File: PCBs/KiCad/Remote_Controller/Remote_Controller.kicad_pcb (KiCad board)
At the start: 4 copper layers, 81 parts, among them J201 USB_C_Receptacle_USB2.0_16P, Q101 IRF7319, Q102 IRFML8244TRPBF, Q103 IRFML8244TRPBF, Q201 SS8050-G, Q202 SS8050-G, SW101 Power Switch, SW201 SW_Push, SW301 SW_Push, SW302 SW_Push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

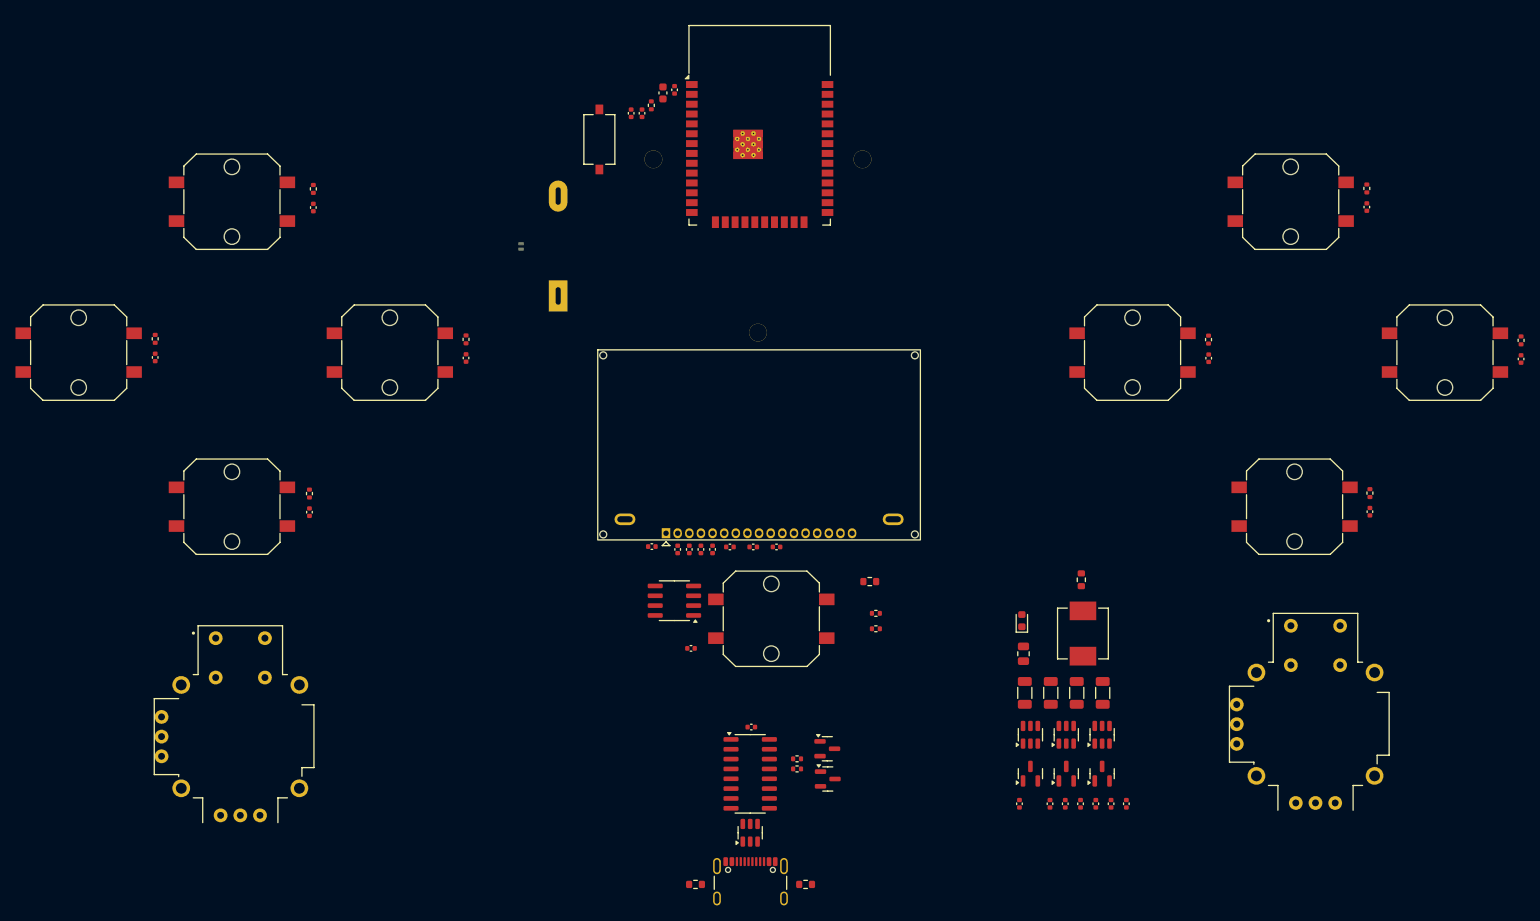
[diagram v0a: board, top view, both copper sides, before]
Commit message: Laid out components and PCB shape
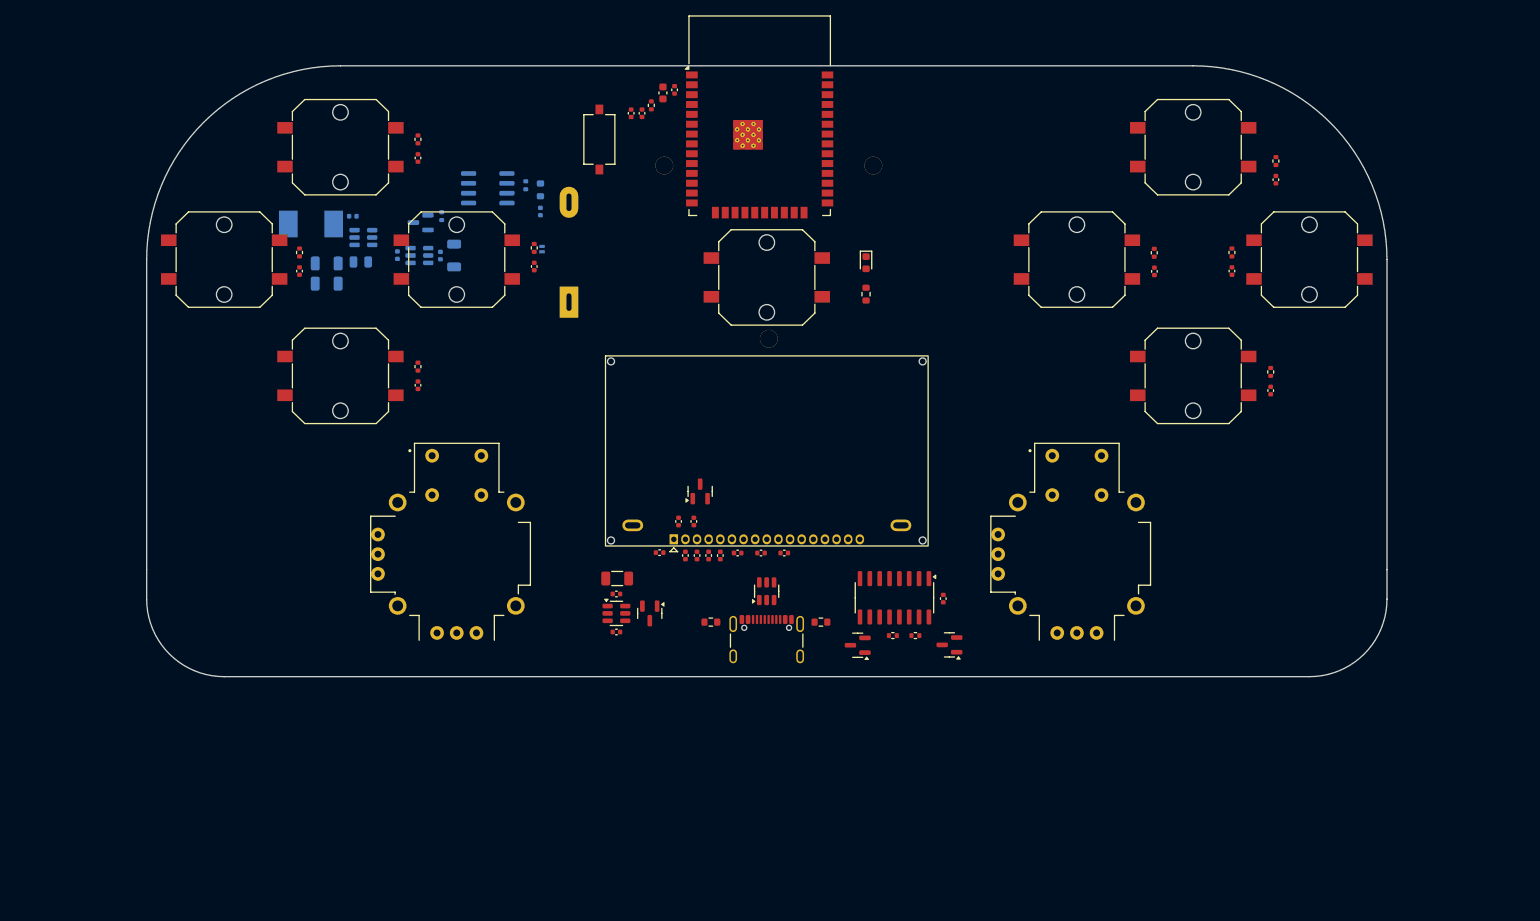
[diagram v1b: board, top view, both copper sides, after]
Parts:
- C101, C102, C103, C104, C105, C106, C107, C108, L101, Q101, Q102, R101, R102, R103, U101, U102: moved to B.Cu
- moved C101 114.6 mm to (87.6, 65.4), turned to 0 degrees
- moved L101 112.7 mm to (82.2, 66.4), turned to 180 degrees
- moved C106 110.0 mm to (93.3, 70.4), turned to -90 degrees
- moved C105 108.6 mm to (84.2, 71.5), turned to 0 degrees
- moved U101 107.3 mm to (89.0, 68.2), turned to 180 degrees
- moved C108 107.2 mm to (98.9, 70.5), turned to -90 degrees
- moved Q102 106.0 mm to (96.3, 66.2), turned to 180 degrees
- moved C104 104.4 mm to (84.2, 74.1), turned to 0 degrees
- moved U102 103.9 mm to (96.2, 70.5), turned to 0 degrees
- moved C103 99.3 mm to (88.6, 71.3), turned to 180 degrees
- moved C107 98.2 mm to (100.7, 70.5), turned to -90 degrees
- moved R102 75.9 mm to (99.1, 65.4), turned to 90 degrees
- moved R101 72.9 mm to (109.9, 61.4), turned to 90 degrees
- moved C113 71.1 mm to (121.6, 114.1), turned to 180 degrees
- moved C111 67.5 mm to (121.6, 119.0), turned to 180 degrees
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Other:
- board outline added: 160 x 78.8 mm

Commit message: Completed more routing and copper pours
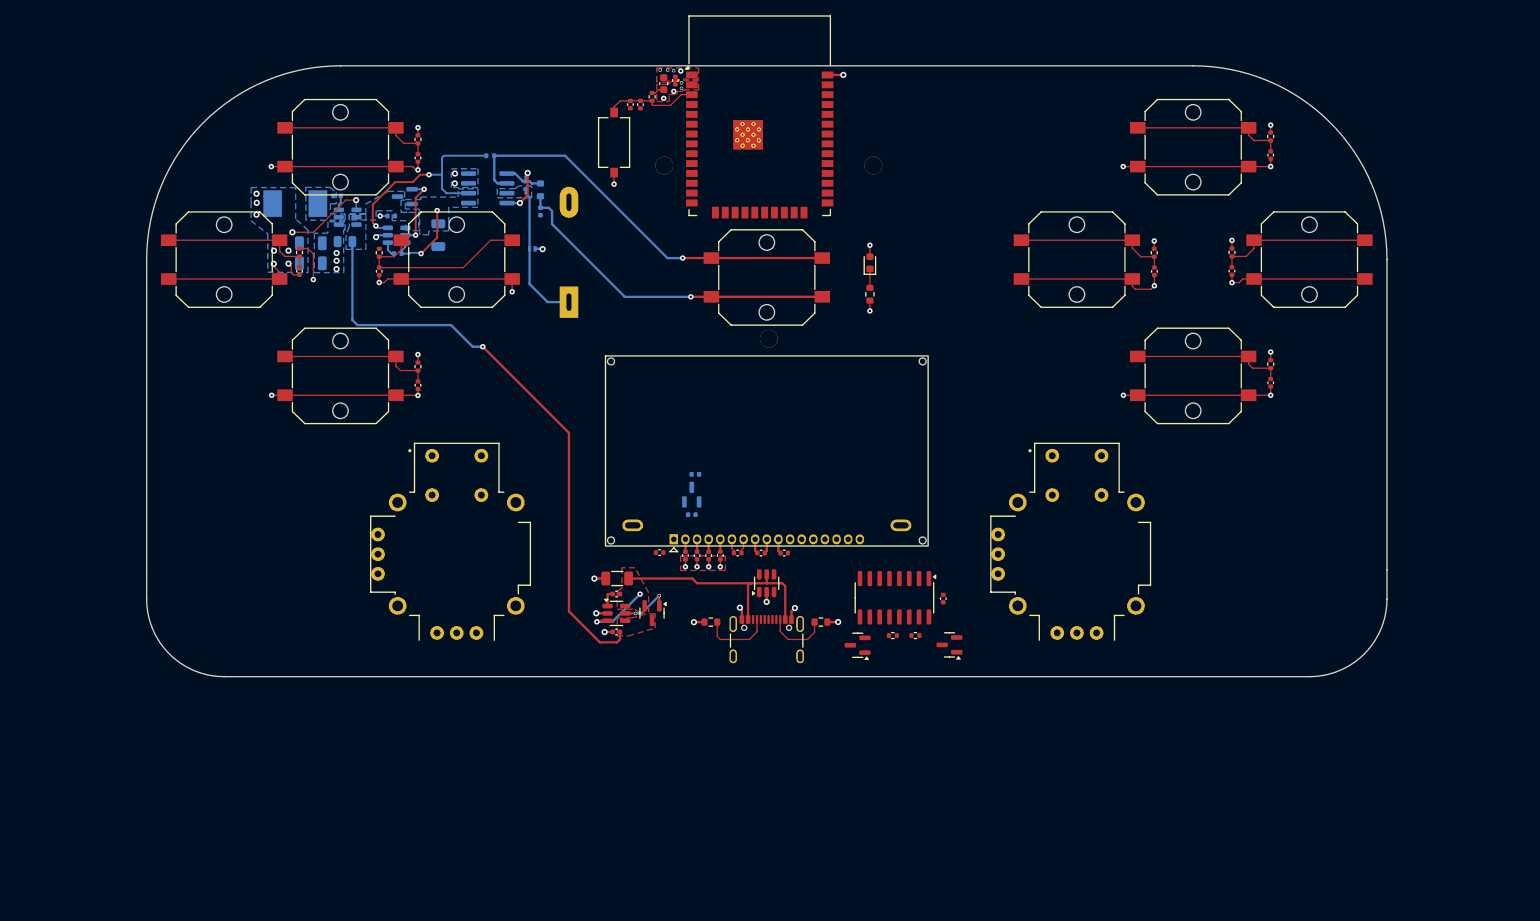
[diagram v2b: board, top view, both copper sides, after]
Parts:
- C109, C110, U103: moved to B.Cu
- moved C315 20.0 mm to (91.0, 72.5)
- moved R307 20.0 mm to (91.0, 70.1)
- moved R102 10.0 mm to (105.3, 57.6), turned to 0 degrees
- moved C109 6.45 mm to (131.8, 98.7), turned to 0 degrees
- moved C108 5.51 mm to (93.4, 70.2), turned to 180 degrees
- moved C106 5.11 mm to (92.5, 65.4), turned to 180 degrees
- moved U102 3.94 mm to (93.2, 67.8)
- moved Q102 3.92 mm to (94.3, 62.9)
- moved C101 3.32 mm to (85.6, 62.8)
- moved C105 3.32 mm to (82.2, 68.9)
- moved C107 3.32 mm to (98.6, 67.8)
- moved L101 3.32 mm to (80.2, 63.8)
- moved U101 3.32 mm to (86.9, 65.5)
- moved C103 3.32 mm to (86.6, 68.7)
- moved C104 3.32 mm to (82.2, 71.5)
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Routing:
- net +3V3: track 0.00 -> 171.6 mm, vias 0 -> 26
- net VCC: track 0.00 -> 76.5 mm, vias 0 -> 1
- net /[1] Power/PW_SW_R: track 0.00 -> 52.7 mm, vias 0 -> 1
- net /[1] Power/PWR_SW_CAP: track 0.00 -> 43.6 mm, vias 0 -> 1
- net VBUS: track 0.00 -> 39.6 mm, vias 0 -> 2
- net /[1] Power/V_Battery: track 0.00 -> 39.2 mm, vias 0 -> 4
- net GND: track 0.00 -> 35.1 mm, vias 0 -> 34
- net FUNC_7: track 0.00 -> 24.5 mm
- net STOP_ROBOT: track 0.00 -> 20.1 mm
- net RECORD_DATA: track 0.00 -> 20.0 mm
- net FUNC_8: track 0.00 -> 20.0 mm
- net CONNECT_BT: track 0.00 -> 20.0 mm
- net FUNC_6: track 0.00 -> 20.0 mm
- net SAVE_DATA: track 0.00 -> 19.8 mm
- net LOCK_ROBOT: track 0.00 -> 19.8 mm
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- added copper zone on In2.Cu, net +3V0
- added copper zone on B.Cu, net +3V3
- added copper zone on F.Cu, net +3V3
- added copper zone on In2.Cu, net +3V3
- added copper zone on B.Cu, net +9V
- added copper zone on B.Cu, net /[1] Power/BUCK_SW
- added copper zone on B.Cu, net /[1] Power/V_Battery
- added copper zone on B.Cu, net GND
- added copper zone on F.Cu, net GND
- added copper zone on In1.Cu, net GND
- added copper zone on F.Cu, net VBUS
- added copper zone on B.Cu, net VCC
- added copper zone on F.Cu, net VCC

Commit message: Changed GPIO connections and completed tracing
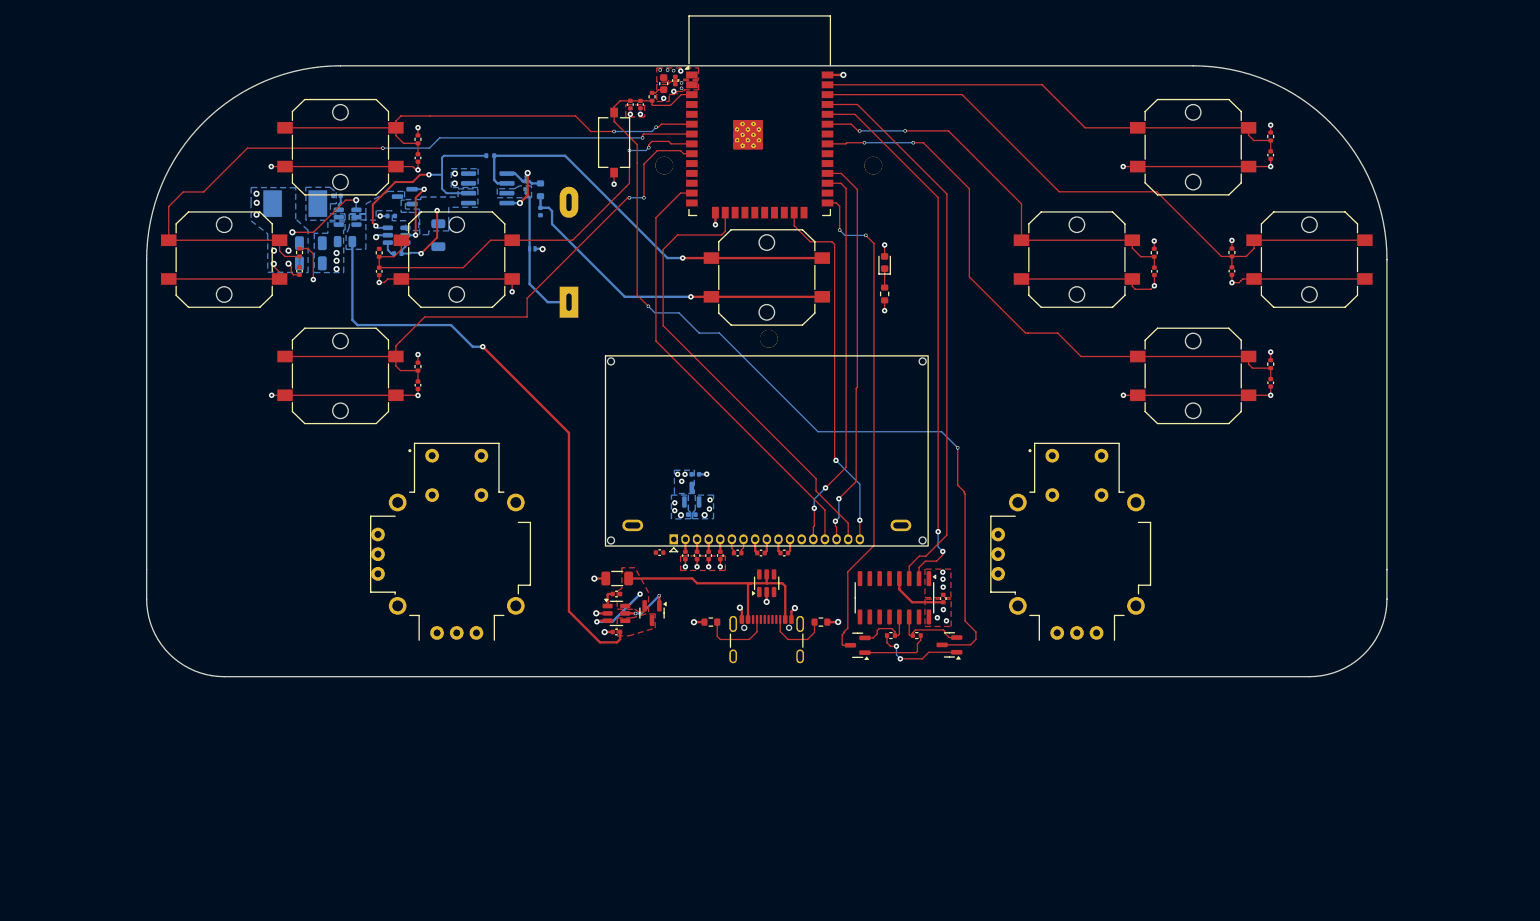
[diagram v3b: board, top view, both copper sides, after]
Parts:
- R104: value 160R -> 200R
- moved D102 1.90 mm to (156.2, 71.4)
- moved R104 1.90 mm to (156.2, 75.4)
- moved R205 0.25 mm to (157.0, 119.5)
- moved R204 0.18 mm to (160.3, 119.5)
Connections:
- U202 pad 10: FUNC_7 -> unconnected-(U202-IO25-Pad10)
- U202 pad 11: FUNC_6 -> unconnected-(U202-IO26-Pad11)
- U202 pad 12: CONNECT_BT -> unconnected-(U202-IO27-Pad12)
- U202 pad 31: unconnected-(U202-IO19-Pad31) -> LOCK_ROBOT
- U202 pad 33: unconnected-(U202-IO21-Pad33) -> RECORD_DATA
- U202 pad 36: unconnected-(U202-IO22-Pad36) -> STOP_ROBOT
- U202 pad 37: FUNC_8 -> SAVE_DATA
- U202 pad 6: RECORD_DATA -> CONNECT_BT
- U202 pad 7: SAVE_DATA -> FUNC_6
- U202 pad 8: LOCK_ROBOT -> FUNC_7
- U202 pad 9: STOP_ROBOT -> FUNC_8
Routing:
- net /[2] Microcontroller And Bluetooth/ENABLE: track 12.2 -> 116.8 mm, vias 0 -> 2
- net FUNC_6: track 20.0 -> 95.9 mm, vias 0 -> 2
- net /[2] Microcontroller And Bluetooth/UART_TX: track 0.00 -> 72.3 mm
- net /[2] Microcontroller And Bluetooth/UART_RX: track 0.00 -> 70.2 mm, vias 0 -> 2
- net /[2] Microcontroller And Bluetooth/IO0: track 0.00 -> 64.5 mm, vias 0 -> 2
- net STOP_ROBOT: track 20.1 -> 80.9 mm
- net /RESET: track 0.00 -> 58.7 mm
- net LOCK_ROBOT: track 19.8 -> 77.9 mm, vias 0 -> 2
- net SPI_CLK: track 0.00 -> 56.5 mm
- net FUNC_8: track 20.0 -> 74.1 mm, vias 0 -> 2
- net REGISTER_SELECT: track 0.00 -> 51.1 mm, vias 0 -> 2
- net SPI_COPI: track 0.00 -> 49.7 mm, vias 0 -> 2
- net /CHIP_SELECT: track 0.00 -> 47.3 mm, vias 0 -> 2
- net SAVE_DATA: track 19.8 -> 62.1 mm
- net CONNECT_BT: track 20.0 -> 60.5 mm, vias 0 -> 2
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- added copper zone on B.Cu, net +3V0

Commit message: Add grounding and stitching vias
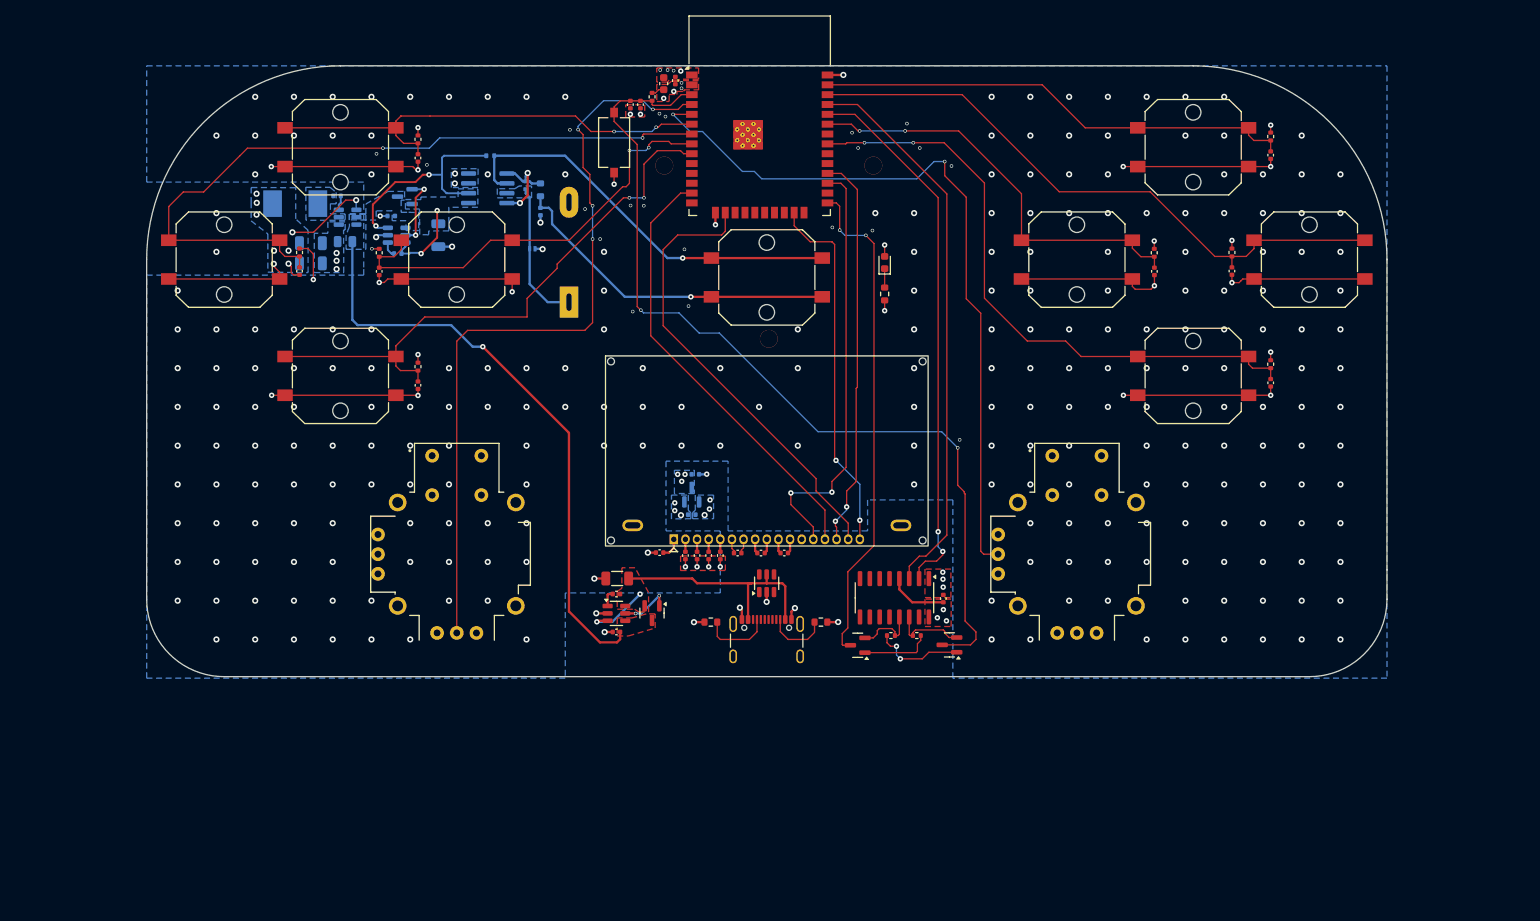
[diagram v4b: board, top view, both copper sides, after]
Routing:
- net LEFT_STICK: track 0.00 -> 99.0 mm, vias 0 -> 4
- net RIGHT_STICK: track 0.00 -> 96.4 mm, vias 0 -> 2
- net SPI_COPI: track 49.7 -> 55.1 mm
- net GND: track 39.6 -> 44.3 mm, vias 44 -> 317
- net /[3] User Interface/LV0: track 0.00 -> 2.72 mm
- net LOCK_ROBOT: track 77.9 -> 80.0 mm
- net /[2] Microcontroller And Bluetooth/ENABLE: track 116.8 -> 117.7 mm
- net RECORD_DATA: track 54.0 -> 54.8 mm
- net SPI_CLK: track 56.5 -> 57.0 mm
